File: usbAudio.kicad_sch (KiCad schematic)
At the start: 51 parts, among them J1 Conn_01x02, J2 USB_C_Receptacle_USB2.0_14P, J3 AudioJack3, SW1 PLAY/PAUSE, SW2 NEXT TR., SW3 MUTE, SW4 VOL+, SW5 VOL-, SW6 PREV. TR., SW7 STOP, SW8 SW_SPDT, U1 PCM2706CPJTR, U2 TPS25810RVCR, U3 AP63205WU-7, U4 MIC5504-3.3YM5-TR, Y1 12MHz

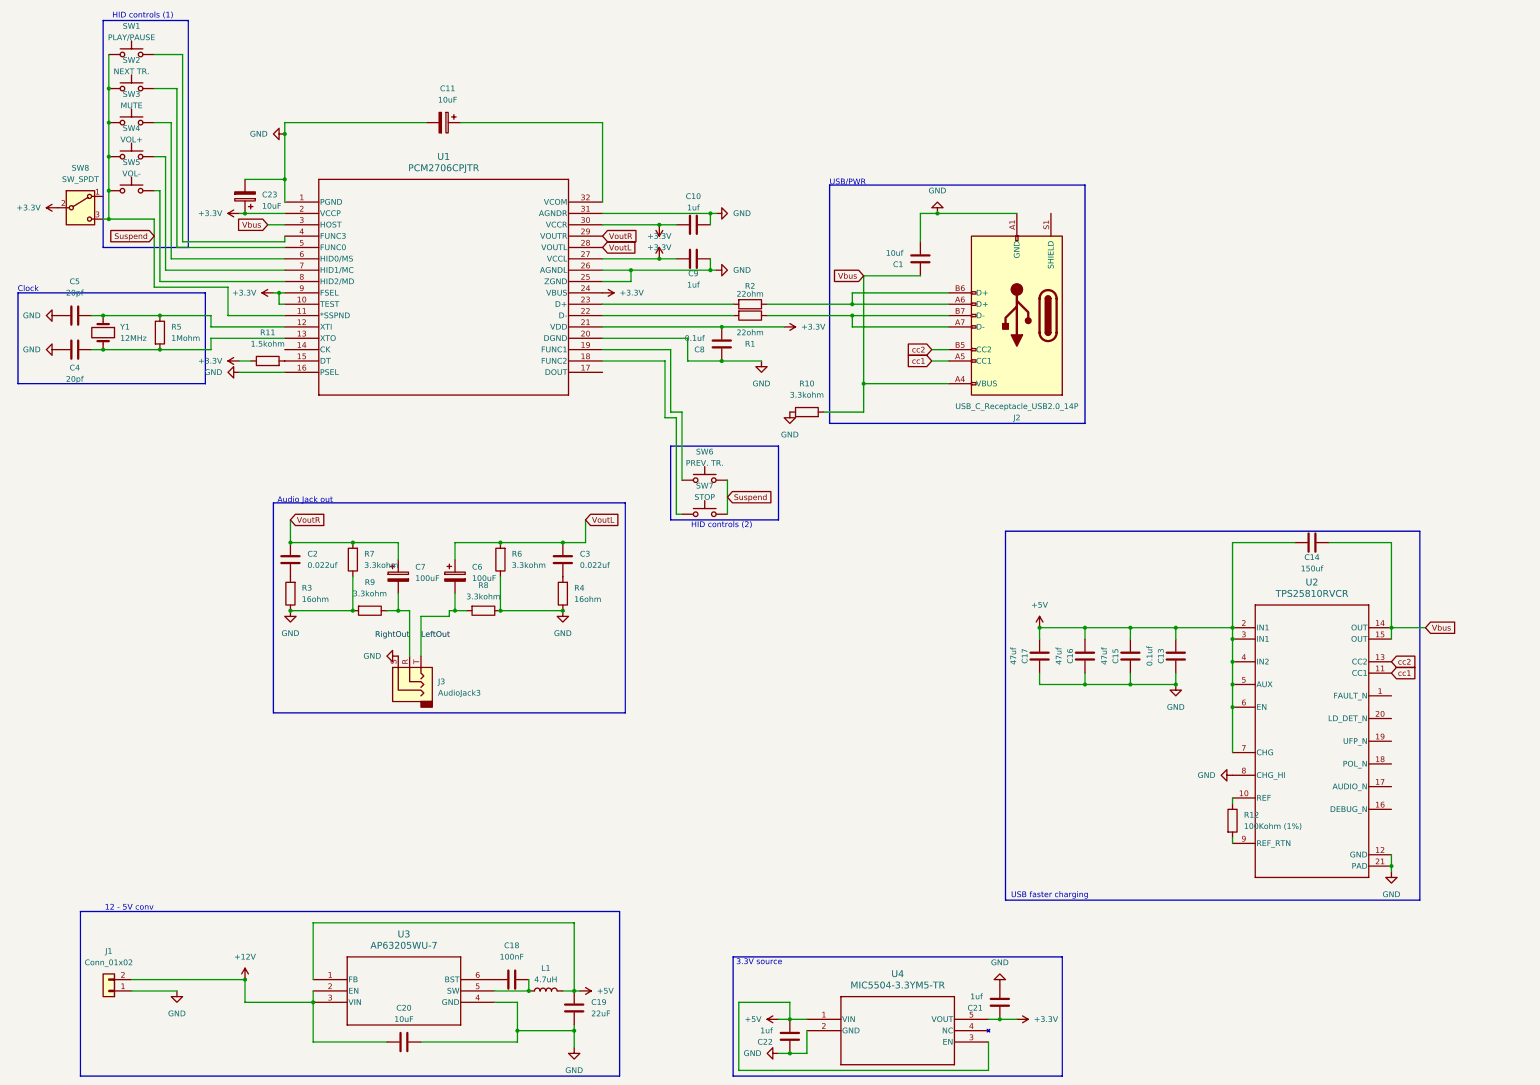
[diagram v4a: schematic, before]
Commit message: Cleaning up and adding footprints
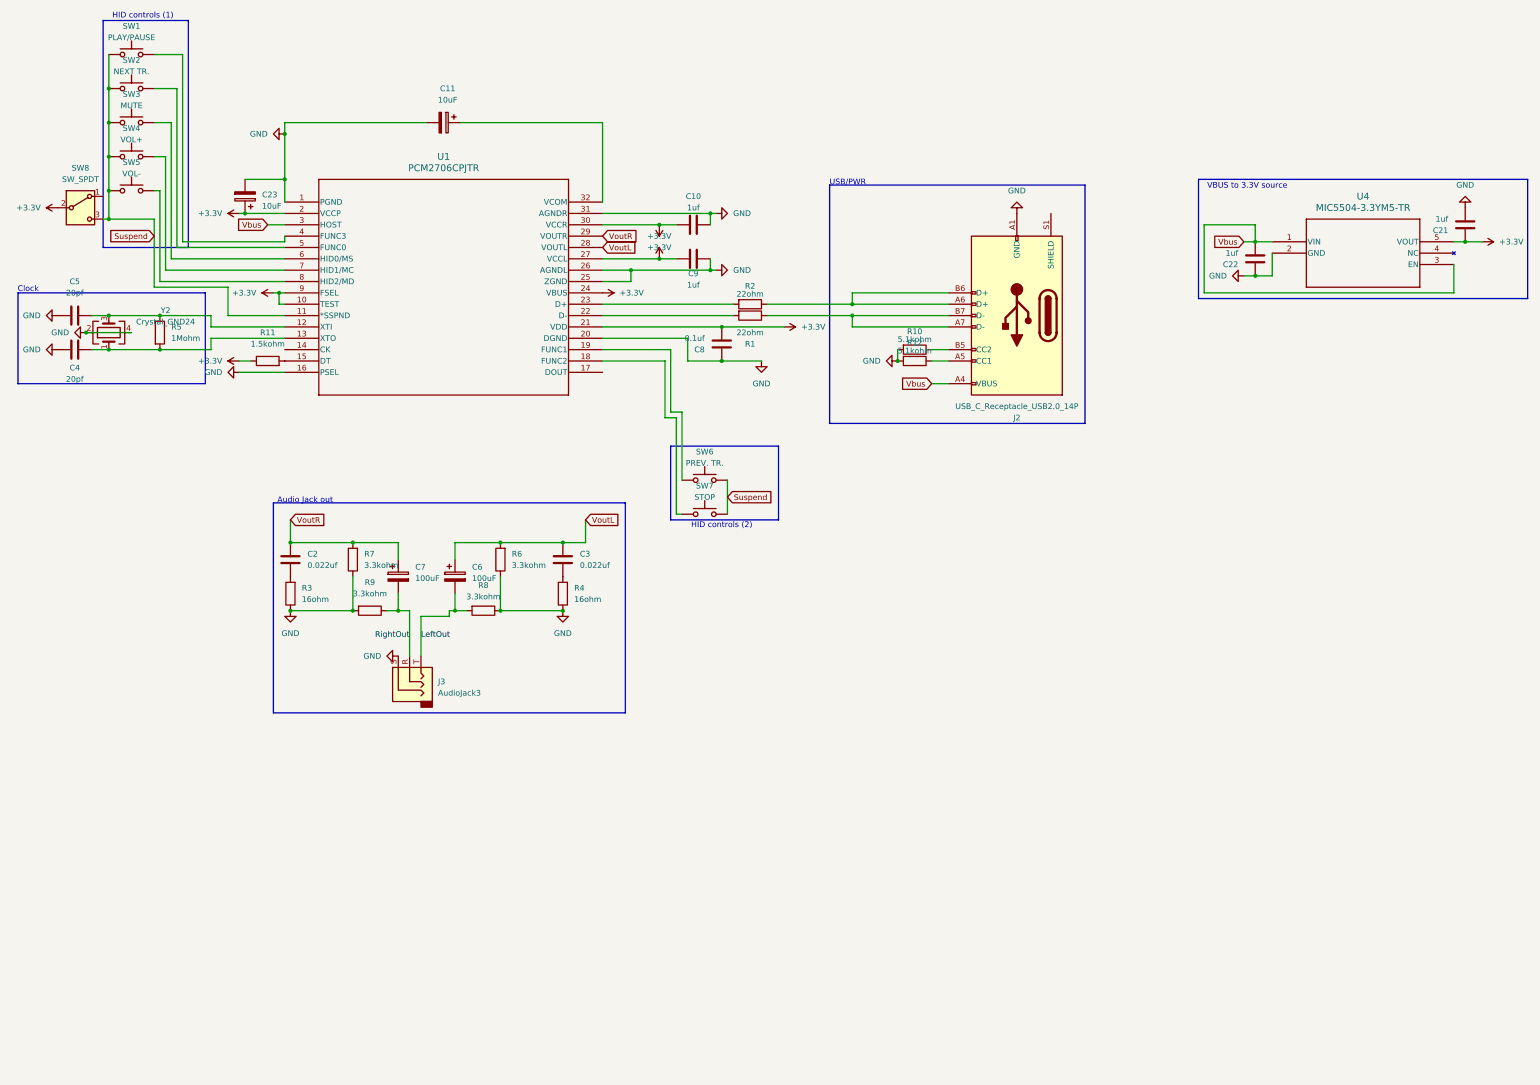
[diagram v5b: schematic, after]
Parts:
- removed C1: 10uf, symbol Device:C
- removed C13: 0.1uf, symbol Device:C
- removed C14: 150uf, symbol Device:C
- removed C15, C16, C17: 47uf, symbol Device:C
- removed C18: 100nF, symbol Device:C
- removed C19: 22uF, symbol Device:C
- removed C20: 10uF, symbol Device:C
- removed J1: Conn_01x02, symbol Connector_Generic:Conn_01x02
- removed L1: 4.7uH, symbol Device:L
- removed U2: TPS25810RVCR, TPS25810:RVC0020A, symbol TPS25810:TPS25810RVCR
- removed U3: AP63205WU-7, AP63205:SOIC_05WU-7_DIO, symbol AP63205:AP63205WU-7
- removed Y1: 12MHz, symbol Device:Crystal
- added Y2: Crystal_GND24, Crystal:Crystal_SMD_3225-4Pin_3.2x2.5mm_HandSoldering, symbol Device:Crystal_GND24
- C2, C3: footprint (none) -> Capacitor_SMD:C_0805_2012Metric_Pad1.18x1.45mm_HandSolder
- C4, C5: footprint (none) -> Capacitor_SMD:C_0603_1608Metric_Pad1.08x0.95mm_HandSolder
- J2: footprint (none) -> Connector_USB:USB_C_Receptacle_HCTL_HC-TYPE-C-16P-01A
- J3: footprint (none) -> Connector_Audio:Jack_3.5mm_KoreanHropartsElec_PJ-320D-4A_Horizontal
- R1, R11, R2, R3, R4, R5, R6, R7, R8, R9: footprint (none) -> Resistor_SMD:R_0603_1608Metric_Pad0.98x0.95mm_HandSolder
- R10: value 3.3kohm -> 5.1kohm; footprint (none) -> Resistor_SMD:R_0603_1608Metric_Pad0.98x0.95mm_HandSolder
- R12: value 100Kohm (1%) -> 5.1kohm; footprint (none) -> Resistor_SMD:R_0603_1608Metric_Pad0.98x0.95mm_HandSolder
- SW1, SW2, SW3, SW4, SW5, SW6, SW7, SW8: footprint (none) -> Button_Switch_THT:SW_PUSH_6mm_H4.3mm
- U1: footprint (none) -> PCM270xC:PJT32
- U4: footprint SOT-23-5_MC_MCH -> MIC5504-3.3YM5:SOT-23-5_MC_MCH
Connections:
- net +5V is gone; now on net Vbus: C22.1, U4.1 (VIN), U4.3 (EN)
- net cc1 is gone; now on an unnamed net: J2.A5 (CC1)
- net GND: now also R10.2, R12.2, Y2.2, Y2.4; no longer R10.1
- net Vbus: no longer R10.2
- net at C5.1, R5.1, U1.12 (XTI): now also Y2.3
- net at C4.1, R5.2, U1.13 (XTO): now also Y2.1
- net cc2: no longer names the net of J2.B5 (CC2)
- net cc2: now also R10.1
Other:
- note added: "VBUS to 3.3V source"
- note removed: "12 - 5V conv"
- note removed: "3.3V source"
- note removed: "USB faster charging"
- moved on the sheet: C21, C22, U4

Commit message: Start work on PCB itself
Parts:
- removed SW3: MUTE, Button_Switch_THT:SW_PUSH_6mm_H4.3mm, symbol Switch:SW_Push
- removed SW6: PREV. TR., Button_Switch_THT:SW_PUSH_6mm_H4.3mm, symbol Switch:SW_Push
- removed SW7: STOP, Button_Switch_THT:SW_PUSH_6mm_H4.3mm, symbol Switch:SW_Push
- C10, C21, C22, C8, C9: footprint (none) -> Capacitor_SMD:C_0603_1608Metric_Pad1.08x0.95mm_HandSolder
- C11, C23: footprint (none) -> Capacitor_THT:CP_Radial_D5.0mm_P2.00mm
- C6, C7: footprint (none) -> Capacitor_THT:CP_Radial_D6.3mm_P2.50mm
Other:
- note removed: "HID controls (2)"
- moved on the sheet: C2, C21, C22, C3, C6, C7, J3, R3, R4, R6, R7, R8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

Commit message: Layout time!!!
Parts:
- J3: footprint Connector_Audio:Jack_3.5mm_KoreanHropartsElec_PJ-320D-4A_Horizontal -> customJack:Jack_3.5mm_KoreanHropartsElec_PJ-320D-4A_Horizontal_copy
- SW8: footprint Button_Switch_THT:SW_PUSH_6mm_H4.3mm -> JS102011SAQN:SW_JS102011SAQN
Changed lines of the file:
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@@
 			)
 		)
-		(property "Footprint" "Connector_Audio:Jack_3.5mm_KoreanHropartsElec_PJ-320D-4A_Horizontal"
+		(property "Footprint" "customJack:Jack_3.5mm_KoreanHropartsElec_PJ-320D-4A_Horizontal_copy"
 			(at 85.09 142.24 0)
 			(effects
@@
 			)
 		)
-		(property "Footprint" "Button_Switch_THT:SW_PUSH_6mm_H4.3mm"
+		(property "Footprint" "JS102011SAQN:SW_JS102011SAQN"
 			(at 26.67 57.15 0)
 			(effects

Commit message: Make more dense!!!!
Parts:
- removed SW2: NEXT TR., Button_Switch_THT:SW_PUSH_6mm_H4.3mm, symbol Switch:SW_Push
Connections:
- net +3.3V: now also U1.3 (HOST)
- net Vbus: no longer U1.3 (HOST)
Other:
- moved on the sheet: SW1
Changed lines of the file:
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@@
 	)
 	(junction
-		(at 33.02 38.1)
-		(diameter 0)
-		(color 0 0 0 0)
-	)
-	(junction
 		(at 170.18 83.82)
 		(diameter 0)
@@
 	(wire
 		(pts
-			(xy 33.02 38.1) (xy 33.02 45.72)
-		)
-		(stroke
-			(width 0)
-			(type default)
-		)
-	)
-	(wire
-		(pts
-			(xy 43.18 38.1) (xy 48.26 38.1)
-		)
-		(stroke
-			(width 0)
-			(type default)
-		)
-	)
-	(wire
-		(pts
 			(xy 62.23 58.42) (xy 63.5 58.42)
 		)
@@
 	(wire
 		(pts
-			(xy 48.26 66.04) (xy 72.39 66.04)
-		)
-		(stroke
-			(width 0)
-			(type default)
-		)
-	)
-	(wire
-		(pts
-			(xy 33.02 30.48) (xy 33.02 38.1)
+			(xy 33.02 38.1) (xy 33.02 45.72)
 		)
 		(stroke
@@
 	(wire
 		(pts
-			(xy 48.26 38.1) (xy 48.26 66.04)
-		)
-		(stroke
-			(width 0)
-			(type default)
-		)
-	)
-	(wire
-		(pts
 			(xy 87.63 127) (xy 95.25 127)
 		)
@@
 	(wire
 		(pts
-			(xy 68.58 60.96) (xy 72.39 60.96)
-		)
-		(stroke
-			(width 0)
-			(type default)
-		)
-	)
-	(wire
-		(pts
 			(xy 167.64 68.58) (xy 167.64 71.12)
 		)
@@
 	(wire
 		(pts
-			(xy 49.53 30.48) (xy 49.53 64.77)
+			(xy 49.53 38.1) (xy 49.53 64.77)
 		)
 		(stroke
@@
 	(wire
 		(pts
+			(xy 63.5 60.96) (xy 63.5 58.42)
+		)
+		(stroke
+			(width 0)
+			(type default)
+		)
+	)
+	(wire
+		(pts
 			(xy 63.5 58.42) (xy 72.39 58.42)
 		)
@@
 	(wire
 		(pts
-			(xy 43.18 30.48) (xy 49.53 30.48)
+			(xy 43.18 38.1) (xy 49.53 38.1)
 		)
 		(stroke
@@
 	(wire
 		(pts
+			(xy 63.5 60.96) (xy 72.39 60.96)
+		)
+		(stroke
+			(width 0)
+			(type default)
+		)
+	)
+	(wire
+		(pts
 			(xy 58.42 127) (xy 72.39 127)
 		)
@@
 	)
 	(rectangle
-		(start 31.75 22.86)
+		(start 31.75 30.48)
 		(end 50.8 66.04)
 		(stroke
@@
 	(text "HID controls (1)"
 		(exclude_from_sim no)
-		(at 40.64 21.59 0)
+		(at 40.894 29.464 0)
 		(effects
 			(font
@@
 		)
 	)
-	(global_label "Vbus"
-		(shape input)
-		(at 68.58 60.96 180)
-		(fields_autoplaced yes)
-		(effects
-			(font
-				(size 1.27 1.27)
-			)
-			(justify right)
-		)
-		(property "Intersheetrefs" "${INTERSHEET_REFS}"
-			(at 61.1801 60.96 0)
-			(effects
-				(font
-					(size 1.27 1.27)
-				)
-				(justify right)
-				(hide yes)
-			)
-		)
-	)
 	(global_label "VoutL"
 		(shape input)
@@
 	(symbol
 		(lib_id "Switch:SW_Push")
-		(at 38.1 30.48 0)
+		(at 38.1 38.1 0)
 		(unit 1)
 		(exclude_from_sim no)
@@
 		(dnp no)
 		(property "Reference" "SW1"
-			(at 38.1 24.13 0)
+			(at 38.1 31.75 0)
 			(effects
 				(font
@@
 		)
 		(property "Value" "PLAY/PAUSE"
-			(at 38.1 26.67 0)
+			(at 38.1 34.29 0)
 			(effects
 				(font
@@
 		)
 		(property "Footprint" "Button_Switch_THT:SW_PUSH_6mm_H4.3mm"
-			(at 38.1 25.4 0)
+			(at 38.1 33.02 0)
 			(effects
 				(font
@@
 		)
 		(property "Datasheet" "~"
-			(at 38.1 25.4 0)
+			(at 38.1 33.02 0)
 			(effects
 				(font
@@
 		)
 		(property "Description" "Push button switch, generic, two pins"
-			(at 38.1 30.48 0)
+			(at 38.1 38.1 0)
 			(effects
 				(font
@@
 					(unit 1)
 				)
-			)
-		)
-	)
-	(symbol
-		(lib_id "Switch:SW_Push")
-		(at 38.1 38.1 0)
-		(unit 1)
-		(exclude_from_sim no)
-		(in_bom yes)
-		(on_board yes)
-		(dnp no)
-		(property "Reference" "SW2"
-			(at 38.1 31.75 0)
-			(effects
-				(font
-					(size 1.27 1.27)
-				)
-			)
-		)
-		(property "Value" "NEXT TR."
-			(at 38.1 34.29 0)
-			(effects
-				(font
-					(size 1.27 1.27)
-				)
-			)
-		)
-		(property "Footprint" "Button_Switch_THT:SW_PUSH_6mm_H4.3mm"
-			(at 38.1 33.02 0)
-			(effects
-				(font
-					(size 1.27 1.27)
-				)
-				(hide yes)
-			)
-		)
-		(property "Datasheet" "~"
-			(at 38.1 33.02 0)
-			(effects
-				(font
-					(size 1.27 1.27)
-				)
-				(hide yes)
-			)
-		)
-		(property "Description" "Push button switch, generic, two pins"
-			(at 38.1 38.1 0)
-			(effects
-				(font
-					(size 1.27 1.27)
-				)
-				(hide yes)
-			)
-		)
-		(pin "2"
-		)
-		(pin "1"
-		)
-		(instances
-			(project "usbAudio"
-				(path "/7baf9a31-bee6-4839-b2a0-7d3e1eb81c1f"
-					(reference "SW2")
-					(unit 1)
-				)
